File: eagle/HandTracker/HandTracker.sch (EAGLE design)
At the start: 26 parts, among them IC1 FT232RL, J1 ZX62-AB-5PA(31), U1 LSM9DS1TR, U2 MAX11629EEE+21-0055_E16+5_MXM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

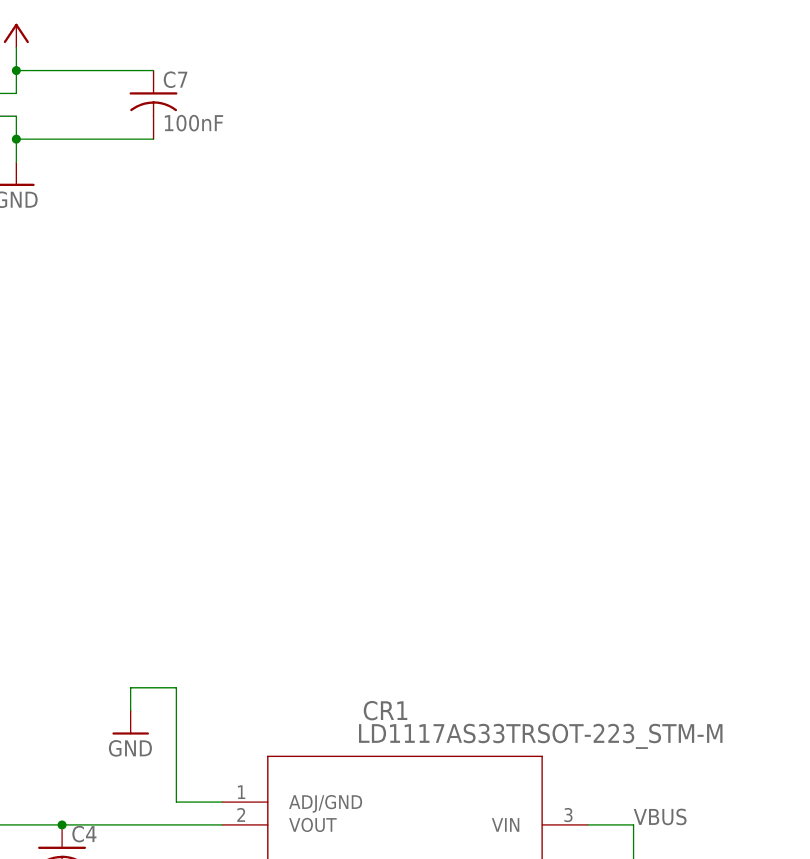
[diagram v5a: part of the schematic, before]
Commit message: added led, completed schematic
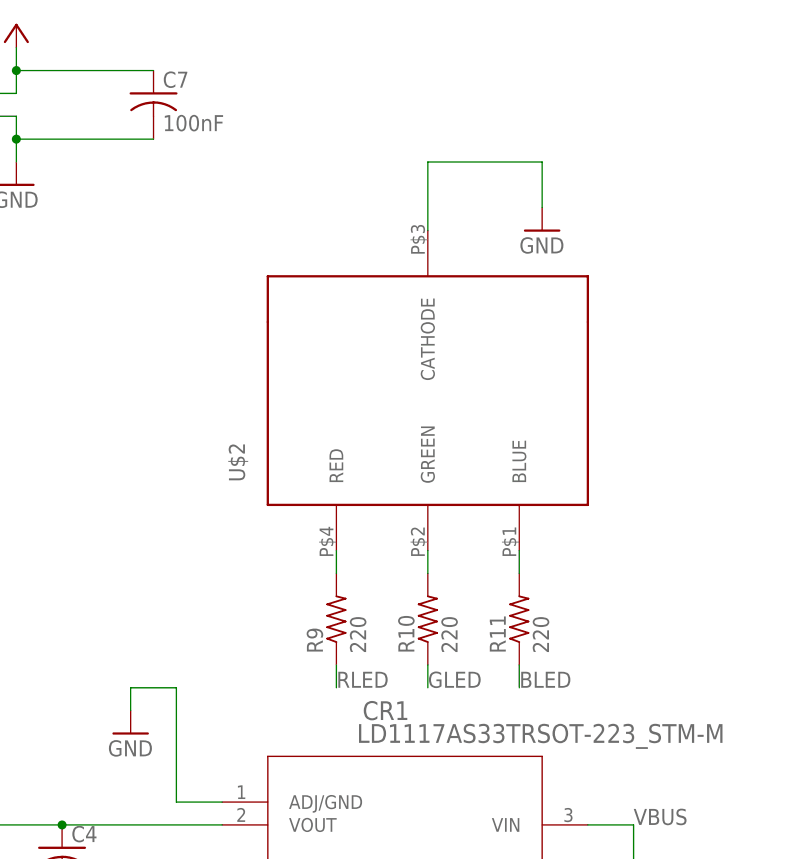
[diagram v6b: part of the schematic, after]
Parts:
- added R10, R11, R9: 220, rcl:R-US_R1206
- added U$2: NTE30158, RGB LED:NTE30158
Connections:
- net BLED: now also R11.1, R11.2, U$2.BLUE
- net GLED: now also R10.1, R10.2, U$2.GREEN
- net GND: now also U$2.CATHODE
- net RLED: now also R9.1, R9.2, U$2.RED
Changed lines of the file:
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@@
 <part name="R3" library="rcl" library_urn="urn:adsk.eagle:library:334" deviceset="R-US_" device="R1206" package3d_urn="urn:adsk.eagle:package:23540/2" value="47k"/>
 <part name="P+13" library="supply1" library_urn="urn:adsk.eagle:library:371" deviceset="VCC" device=""/>
+<part name="U$2" library="RGB LED" deviceset="NTE30158" device=""/>
+<part name="GND14" library="supply1" library_urn="urn:adsk.eagle:library:371" deviceset="GND" device=""/>
+<part name="R9" library="rcl" library_urn="urn:adsk.eagle:library:334" deviceset="R-US_" device="R1206" package3d_urn="urn:adsk.eagle:package:23540/2" value="220"/>
+<part name="R10" library="rcl" library_urn="urn:adsk.eagle:library:334" deviceset="R-US_" device="R1206" package3d_urn="urn:adsk.eagle:package:23540/2" value="220"/>
+<part name="R11" library="rcl" library_urn="urn:adsk.eagle:library:334" deviceset="R-US_" device="R1206" package3d_urn="urn:adsk.eagle:package:23540/2" value="220"/>
 </parts>
 <sheets>
@@
 <instance part="P+13" gate="VCC" x="-30.48" y="63.5" smashed="yes">
 <attribute name="VALUE" x="-33.02" y="60.96" size="1.778" layer="96" rot="R90"/>
+</instance>
+<instance part="U$2" gate="G$1" x="147.32" y="22.86" smashed="yes">
+<attribute name="NAME" x="144.78" y="25.4" size="1.778" layer="95" rot="R90"/>
+</instance>
+<instance part="GND14" gate="1" x="177.8" y="53.34" smashed="yes">
+<attribute name="VALUE" x="175.26" y="50.8" size="1.778" layer="96"/>
+</instance>
+<instance part="R9" gate="G$1" x="154.94" y="10.16" smashed="yes" rot="R90">
+<attribute name="NAME" x="153.4414" y="6.35" size="1.778" layer="95" rot="R90"/>
+<attribute name="VALUE" x="158.242" y="6.35" size="1.778" layer="96" rot="R90"/>
+</instance>
+<instance part="R10" gate="G$1" x="165.1" y="10.16" smashed="yes" rot="R90">
+<attribute name="NAME" x="163.6014" y="6.35" size="1.778" layer="95" rot="R90"/>
+<attribute name="VALUE" x="168.402" y="6.35" size="1.778" layer="96" rot="R90"/>
+</instance>
+<instance part="R11" gate="G$1" x="175.26" y="10.16" smashed="yes" rot="R90">
+<attribute name="NAME" x="173.7614" y="6.35" size="1.778" layer="95" rot="R90"/>
+<attribute name="VALUE" x="178.562" y="6.35" size="1.778" layer="96" rot="R90"/>
 </instance>
 </instances>
@@
 <junction x="-38.1" y="33.02"/>
 </segment>
+<segment>
+<pinref part="GND14" gate="1" pin="GND"/>
+<wire x1="177.8" y1="55.88" x2="177.8" y2="60.96" width="0.1524" layer="91"/>
+<wire x1="177.8" y1="60.96" x2="165.1" y2="60.96" width="0.1524" layer="91"/>
+<pinref part="U$2" gate="G$1" pin="CATHODE"/>
+<wire x1="165.1" y1="60.96" x2="165.1" y2="53.34" width="0.1524" layer="91"/>
+</segment>
 </net>
 <net name="VBUS" class="0">
@@
 <label x="81.28" y="-27.94" size="1.778" layer="95"/>
 </segment>
+<segment>
+<pinref part="U$2" gate="G$1" pin="RED"/>
+<wire x1="154.94" y1="17.78" x2="154.94" y2="15.24" width="0.1524" layer="91"/>
+<pinref part="R9" gate="G$1" pin="2"/>
+</segment>
+<segment>
+<pinref part="R9" gate="G$1" pin="1"/>
+<wire x1="154.94" y1="5.08" x2="154.94" y2="2.54" width="0.1524" layer="91"/>
+<label x="154.94" y="2.54" size="1.778" layer="95"/>
+</segment>
 </net>
 <net name="GLED" class="0">
@@
 <label x="81.28" y="-30.48" size="1.778" layer="95"/>
 </segment>
+<segment>
+<pinref part="U$2" gate="G$1" pin="GREEN"/>
+<wire x1="165.1" y1="17.78" x2="165.1" y2="15.24" width="0.1524" layer="91"/>
+<pinref part="R10" gate="G$1" pin="2"/>
+</segment>
+<segment>
+<pinref part="R10" gate="G$1" pin="1"/>
+<wire x1="165.1" y1="5.08" x2="165.1" y2="2.54" width="0.1524" layer="91"/>
+<label x="165.1" y="2.54" size="1.778" layer="95"/>
+</segment>
 </net>
 <net name="BLED" class="0">
@@
 <label x="25.4" y="-33.02" size="1.778" layer="95"/>
 </segment>
-</net>
+<segment>
+<pinref part="U$2" gate="G$1" pin="BLUE"/>
+<wire x1="175.26" y1="17.78" x2="175.26" y2="15.24" width="0.1524" layer="91"/>
+<pinref part="R11" gate="G$1" pin="2"/>
+</segment>
+<segment>
+<pinref part="R11" gate="G$1" pin="1"/>
+<wire x1="175.26" y1="5.08" x2="175.26" y2="2.54" width="0.1524" layer="91"/>
+<label x="175.26" y="2.54" size="1.778" layer="95"/>
+</segment>
+</net>

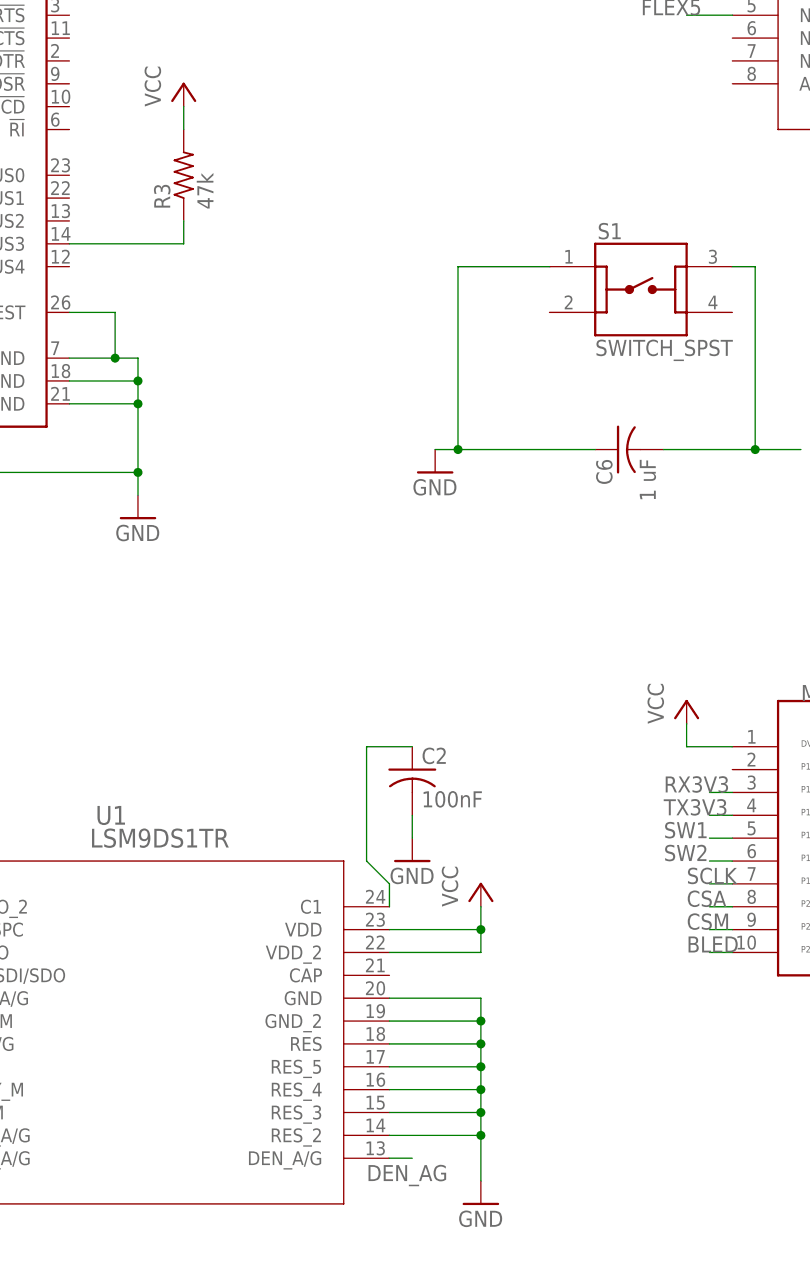
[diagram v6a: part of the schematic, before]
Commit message: updated passive component values to reflect recommended operating conditions for various ICs
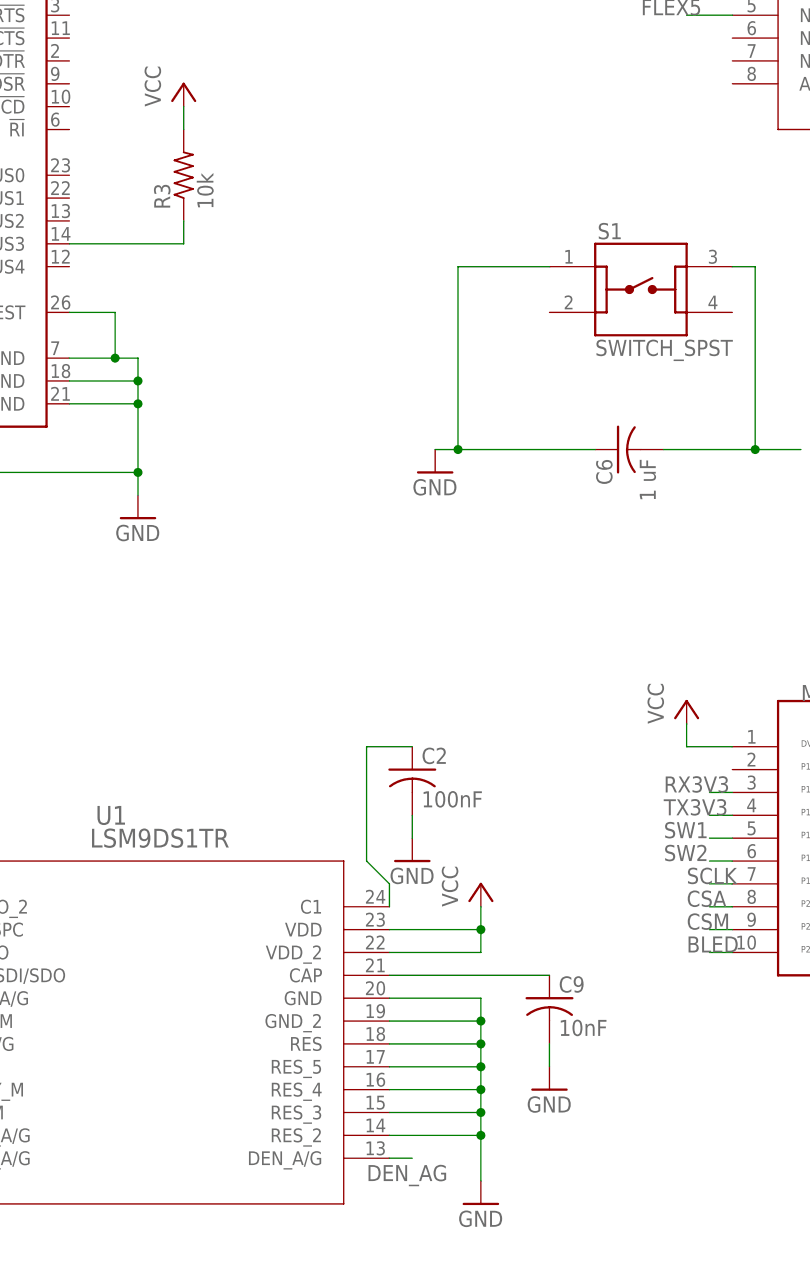
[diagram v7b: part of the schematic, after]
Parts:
- added C9: 10nF, rcl:C-USC1206
- R3: value 47k -> 10k
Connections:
- new net N$6: C9.1, U1.CAP
- net GND: now also C9.2
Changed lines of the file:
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@@
 <part name="GND13" library="supply1" library_urn="urn:adsk.eagle:library:371" deviceset="GND" device=""/>
 <part name="P+7" library="supply1" library_urn="urn:adsk.eagle:library:371" deviceset="VCC" device=""/>
-<part name="R3" library="rcl" library_urn="urn:adsk.eagle:library:334" deviceset="R-US_" device="R1206" package3d_urn="urn:adsk.eagle:package:23540/2" value="47k"/>
+<part name="R3" library="rcl" library_urn="urn:adsk.eagle:library:334" deviceset="R-US_" device="R1206" package3d_urn="urn:adsk.eagle:package:23540/2" value="10k"/>
 <part name="P+13" library="supply1" library_urn="urn:adsk.eagle:library:371" deviceset="VCC" device=""/>
 <part name="U$2" library="RGB LED" deviceset="NTE30158" device=""/>
@@
 <part name="R10" library="rcl" library_urn="urn:adsk.eagle:library:334" deviceset="R-US_" device="R1206" package3d_urn="urn:adsk.eagle:package:23540/2" value="220"/>
 <part name="R11" library="rcl" library_urn="urn:adsk.eagle:library:334" deviceset="R-US_" device="R1206" package3d_urn="urn:adsk.eagle:package:23540/2" value="220"/>
+<part name="C9" library="rcl" library_urn="urn:adsk.eagle:library:334" deviceset="C-US" device="C1206" package3d_urn="urn:adsk.eagle:package:23618/2" value="10nF"/>
+<part name="GND15" library="supply1" library_urn="urn:adsk.eagle:library:371" deviceset="GND" device=""/>
 </parts>
 <sheets>
@@
 <attribute name="NAME" x="173.7614" y="6.35" size="1.778" layer="95" rot="R90"/>
 <attribute name="VALUE" x="178.562" y="6.35" size="1.778" layer="96" rot="R90"/>
+</instance>
+<instance part="C9" gate="G$1" x="10.16" y="-38.1" smashed="yes">
+<attribute name="NAME" x="11.176" y="-37.465" size="1.778" layer="95"/>
+<attribute name="VALUE" x="11.176" y="-42.291" size="1.778" layer="96"/>
+</instance>
+<instance part="GND15" gate="1" x="10.16" y="-48.26" smashed="yes">
+<attribute name="VALUE" x="7.62" y="-50.8" size="1.778" layer="96"/>
 </instance>
 </instances>
@@
 <wire x1="165.1" y1="60.96" x2="165.1" y2="53.34" width="0.1524" layer="91"/>
 </segment>
+<segment>
+<pinref part="C9" gate="G$1" pin="2"/>
+<wire x1="10.16" y1="-43.18" x2="10.16" y2="-45.72" width="0.1524" layer="91"/>
+<pinref part="GND15" gate="1" pin="GND"/>
+</segment>
 </net>
 <net name="VBUS" class="0">
@@
 </segment>
 </net>
+<net name="N$6" class="0">
+<segment>
+<pinref part="C9" gate="G$1" pin="1"/>
+<pinref part="U1" gate="A" pin="CAP"/>
+<wire x1="10.16" y1="-35.56" x2="-7.62" y2="-35.56" width="0.1524" layer="91"/>
+</segment>
+</net>

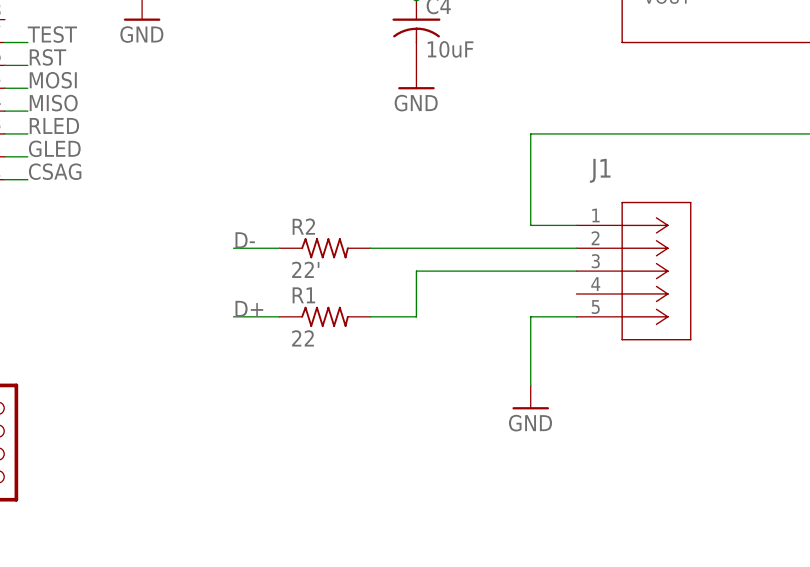
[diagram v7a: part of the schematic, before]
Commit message: removed USB termination resistors
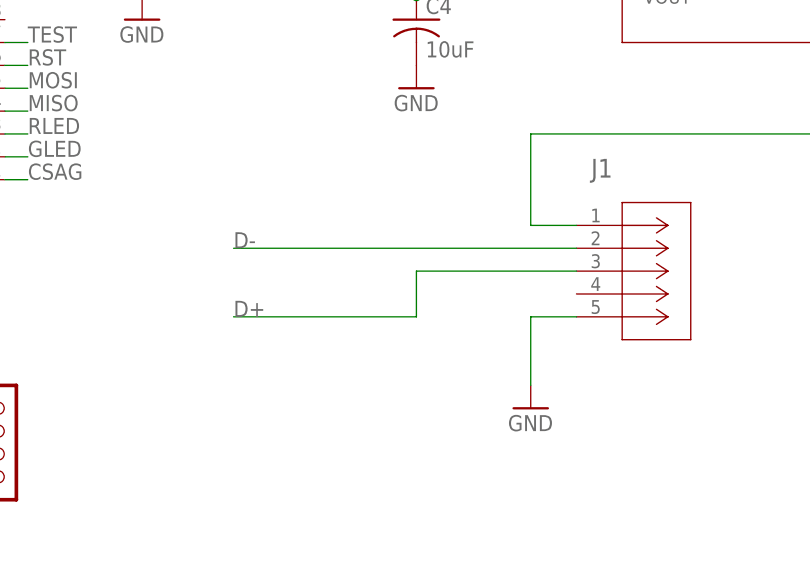
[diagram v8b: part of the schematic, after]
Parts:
- removed R1: 22, rcl:R-US_R1206
- removed R2: 22', rcl:R-US_R1206
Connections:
- removed net N$2: J1.D+, R1.2
- removed net N$5: J1.D-, R2.2
- net D+: now also J1.D+; no longer R1.1
- net D-: now also J1.D-; no longer R2.1
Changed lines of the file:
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@@
 <part name="C2" library="rcl" library_urn="urn:adsk.eagle:library:334" deviceset="C-US" device="C1206" package3d_urn="urn:adsk.eagle:package:23618/2" value="100nF"/>
 <part name="GND8" library="supply1" library_urn="urn:adsk.eagle:library:371" deviceset="GND" device=""/>
-<part name="R1" library="rcl" library_urn="urn:adsk.eagle:library:334" deviceset="R-US_" device="R1206" package3d_urn="urn:adsk.eagle:package:23540/2" value="22"/>
-<part name="R2" library="rcl" library_urn="urn:adsk.eagle:library:334" deviceset="R-US_" device="R1206" package3d_urn="urn:adsk.eagle:package:23540/2" value="22'"/>
 <part name="JP2" library="pinhead" library_urn="urn:adsk.eagle:library:325" deviceset="PINHD-1X10" device="" package3d_urn="urn:adsk.eagle:package:22406/2"/>
 <part name="GND16" library="supply1" library_urn="urn:adsk.eagle:library:371" deviceset="GND" device=""/>
@@
 <attribute name="VALUE" x="-7.62" y="-25.4" size="1.778" layer="96"/>
 </instance>
-<instance part="R1" gate="G$1" x="114.3" y="-48.26" smashed="yes">
-<attribute name="NAME" x="110.49" y="-46.7614" size="1.778" layer="95"/>
-<attribute name="VALUE" x="110.49" y="-51.562" size="1.778" layer="96"/>
-</instance>
-<instance part="R2" gate="G$1" x="114.3" y="-40.64" smashed="yes">
-<attribute name="NAME" x="110.49" y="-39.1414" size="1.778" layer="95"/>
-<attribute name="VALUE" x="110.49" y="-43.942" size="1.778" layer="96"/>
-</instance>
 <instance part="JP2" gate="A" x="33.02" y="109.22" smashed="yes">
 <attribute name="NAME" x="26.67" y="122.555" size="1.778" layer="95"/>
@@
 <net name="D-" class="0">
 <segment>
-<pinref part="R2" gate="G$1" pin="1"/>
-<wire x1="109.22" y1="-40.64" x2="104.14" y2="-40.64" width="0.1524" layer="91"/>
 <label x="104.14" y="-40.64" size="1.778" layer="95"/>
+<pinref part="J1" gate="A" pin="D-"/>
+<wire x1="104.14" y1="-40.64" x2="142.24" y2="-40.64" width="0.1524" layer="91"/>
 </segment>
 <segment>
@@
 <net name="D+" class="0">
 <segment>
-<pinref part="R1" gate="G$1" pin="1"/>
-<wire x1="109.22" y1="-48.26" x2="104.14" y2="-48.26" width="0.1524" layer="91"/>
 <label x="104.14" y="-48.26" size="1.778" layer="95"/>
+<pinref part="J1" gate="A" pin="D+"/>
+<wire x1="124.46" y1="-48.26" x2="124.46" y2="-43.18" width="0.1524" layer="91"/>
+<wire x1="124.46" y1="-43.18" x2="142.24" y2="-43.18" width="0.1524" layer="91"/>
+<wire x1="104.14" y1="-48.26" x2="124.46" y2="-48.26" width="0.1524" layer="91"/>
 </segment>
 <segment>
@@
 </segment>
 </net>
-<net name="N$2" class="0">
-<segment>
-<pinref part="R1" gate="G$1" pin="2"/>
-<wire x1="119.38" y1="-48.26" x2="124.46" y2="-48.26" width="0.1524" layer="91"/>
-<pinref part="J1" gate="A" pin="D+"/>
-<wire x1="124.46" y1="-48.26" x2="124.46" y2="-43.18" width="0.1524" layer="91"/>
-<wire x1="124.46" y1="-43.18" x2="142.24" y2="-43.18" width="0.1524" layer="91"/>
-</segment>
-</net>
-<net name="N$5" class="0">
-<segment>
-<pinref part="R2" gate="G$1" pin="2"/>
-<pinref part="J1" gate="A" pin="D-"/>
-<wire x1="119.38" y1="-40.64" x2="142.24" y2="-40.64" width="0.1524" layer="91"/>
-</segment>
-</net>
